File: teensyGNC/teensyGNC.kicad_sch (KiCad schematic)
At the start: 42 parts, among them J1 ESC_1_PWM, J10 ToF_OF_SH, J11 Hall_1_PH, J12 Hall_2_PH, J13 Hall_3_PH, J14 Hall_4_PH, J2 5V_In_XH, J3 ESC_2_PWM, J4 Servo_1_PWM, J5 Servo_2_PWM, J6 7V4_In, J7 Ebyte, J8 LC29H, J9 Batt_Mon_GH, U1 E28-2G4T20SX, U2 4754, U3 AP2112K-3.3, U4 4494, U5 Teensy4.1

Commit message: Test fabrication
- Downloaded fabrication toolkit
- Updated LCSC Part --> LCSC Part #
- Test BOM and gerber creation using toolkit
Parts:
- C1, C3: LCSC Part C7234 -> (none); LCSC Part # (none) -> C7234
- C2, C4, C9: LCSC Part C14663 -> (none); LCSC Part # (none) -> C14663
- C5, C6: footprint Capacitor_SMD:C_0402_1005Metric -> Capacitor_SMD:C_0603_1608Metric
- C7: LCSC Part C559769 -> (none); LCSC Part # (none) -> C559769
- C8: LCSC Part C109457 -> (none); LCSC Part # (none) -> C109457
- D1: LCSC Part C135018 -> (none); LCSC Part # (none) -> C135018
- J10: LCSC Part C160390 -> (none); LCSC Part # (none) -> C160390
- J11, J12, J13, J14: LCSC Part C131339 -> (none); LCSC Part # (none) -> C131339
- J2: LCSC Part C158012 -> (none); LCSC Part # (none) -> C158012
- J6: LCSC Part C428721 -> (none); LCSC Part # (none) -> C428721
- J7: LCSC Part C6962402 -> (none); LCSC Part # (none) -> C6962402
- J9: LCSC Part C161692 -> (none); LCSC Part # (none) -> C161692
- R1, R2: LCSC Part C122970 -> (none); LCSC Part # (none) -> C122970
- R10, R11, R5, R6, R7, R8, R9: LCSC Part C5362358 -> (none); LCSC Part # (none) -> C5362358
- R12, R13: LCSC Part C4190 -> (none); LCSC Part # (none) -> C4190
- R3: LCSC Part # (none) -> C5362358
- R4: footprint Resistor_SMD:R_0402_1005Metric -> Resistor_SMD:R_0603_1608Metric; LCSC Part C17168 -> (none); LCSC Part # (none) -> C17168
- U1: LCSC Part C42464206 -> (none); LCSC Part # (none) -> C42464206
- U3: LCSC Part C51118 -> (none); LCSC Part # (none) -> C51118

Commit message: V1.0 Order placed at JLCPCB
- Some components changed to basic versions to lower cost a bit (TOTAL 96 USD!!!?? Do try and lower further for future versions, main cost seems to be extended part fees, maybe look into more hand soldered bits?)
- Some JST connectors bought on taobao and assembled myself
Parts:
- C7: LCSC Part # C559769 -> C29936
- J7: footprint Connector_Coaxial:SMA_Amphenol_132203-12_Horizontal -> Connector_Coaxial:SMA_BAT_Wireless_BWSMA-KWE-Z001; LCSC Part # C6962402 -> C496551
- R10, R11, R3, R5, R6, R7, R8, R9: LCSC Part # C5362358 -> C25804
- R4: LCSC Part # C17168 -> C95177
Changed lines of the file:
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@@
 			)
 		)
-		(property "LCSC Part #" "C17168"
+		(property "LCSC Part #" "C95177"
 			(at 86.36 73.66 90)
 			(hide yes)
@@
 			)
 		)
-		(property "LCSC Part #" "C5362358"
+		(property "LCSC Part #" "C25804"
 			(at 97.79 39.37 90)
 			(hide yes)
@@
 			)
 		)
-		(property "LCSC Part #" "C5362358"
+		(property "LCSC Part #" "C25804"
 			(at 71.12 156.21 90)
 			(hide yes)
@@
 			)
 		)
-		(property "LCSC Part #" "C559769"
+		(property "LCSC Part #" "C29936"
 			(at 115.57 93.98 90)
 			(hide yes)
@@
 			)
 		)
-		(property "LCSC Part #" "C5362358"
+		(property "LCSC Part #" "C25804"
 			(at 121.92 39.37 90)
 			(hide yes)
@@
 			)
 		)
-		(property "LCSC Part #" "C5362358"
+		(property "LCSC Part #" "C25804"
 			(at 88.9 39.37 90)
 			(hide yes)
@@
 			)
 		)
-		(property "LCSC Part #" "C5362358"
+		(property "LCSC Part #" "C25804"
 			(at 132.08 39.37 90)
 			(hide yes)
@@
 			)
 		)
-		(property "LCSC Part #" "C5362358"
+		(property "LCSC Part #" "C25804"
 			(at 124.46 119.38 90)
 			(hide yes)
@@
 			)
 		)
-		(property "Footprint" "Connector_Coaxial:SMA_Amphenol_132203-12_Horizontal"
+		(property "Footprint" "Connector_Coaxial:SMA_BAT_Wireless_BWSMA-KWE-Z001"
 			(at 101.6 73.66 0)
 			(hide yes)
@@
 			)
 		)
-		(property "LCSC Part #" "C6962402"
+		(property "LCSC Part #" "C496551"
 			(at 101.6 73.66 0)
 			(hide yes)
@@
 			)
 		)
-		(property "LCSC Part #" "C5362358"
+		(property "LCSC Part #" "C25804"
 			(at 107.95 39.37 90)
 			(hide yes)
@@
 			)
 		)
-		(property "LCSC Part #" "C5362358"
+		(property "LCSC Part #" "C25804"
 			(at 114.3 119.38 90)
 			(hide yes)

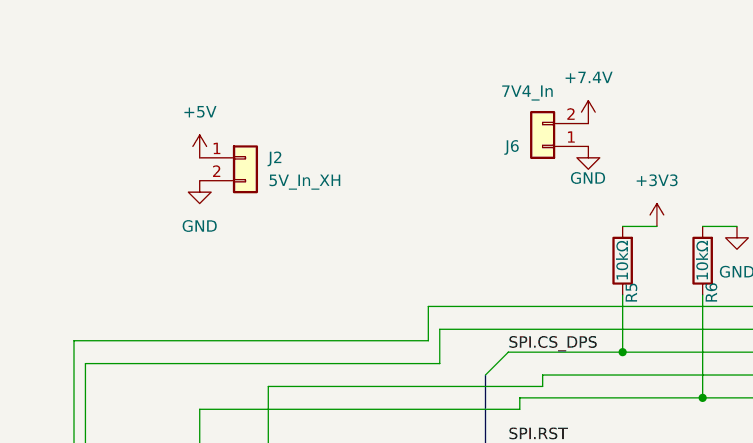
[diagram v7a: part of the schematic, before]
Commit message: ! CRITICAL FIX !
5V Input plug was placed the wrong way around, now flipped back to the correct direction on the board. For the V1.0 deliveries, the first board might have had its ebyte power voltage converter fried (not tested yet), jst xh flipped manually (steps in notebook) for successful testing of altitude control on vehicle. For second board, will need to flip the jst xh first.
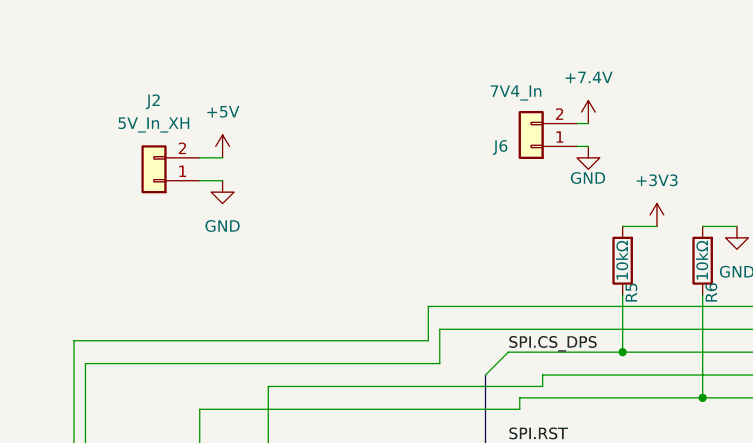
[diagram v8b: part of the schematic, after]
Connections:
- net +5V: now also J2.2 (Pin_2); no longer J2.1 (Pin_1)
- net GND: now also J2.1 (Pin_1); no longer J2.2 (Pin_2)
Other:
- moved on the sheet: J2, J6
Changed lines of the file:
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@@
 	(wire
 		(pts
+			(xy 83.82 24.13) (xy 85.09 24.13)
+		)
+		(stroke
+			(width 0)
+			(type default)
+		)
+	)
+	(wire
+		(pts
 			(xy 78.74 100.33) (xy 78.74 105.41)
 		)
@@
 	(wire
 		(pts
+			(xy 44.45 30.48) (xy 41.91 30.48)
+		)
+		(stroke
+			(width 0)
+			(type default)
+		)
+	)
+	(wire
+		(pts
 			(xy 25.4 172.72) (xy 82.55 172.72)
 		)
@@
 	(wire
 		(pts
+			(xy 44.45 27.94) (xy 41.91 27.94)
+		)
+		(stroke
+			(width 0)
+			(type default)
+		)
+	)
+	(wire
+		(pts
 			(xy 132.08 35.56) (xy 135.89 35.56)
 		)
@@
 	(wire
 		(pts
+			(xy 83.82 26.67) (xy 85.09 26.67)
+		)
+		(stroke
+			(width 0)
+			(type default)
+		)
+	)
+	(wire
+		(pts
 			(xy 213.36 57.15) (xy 213.36 73.66)
 		)
@@
 	(symbol
 		(lib_id "Connector_Generic:Conn_01x02")
-		(at 46.99 27.94 0)
+		(at 36.83 30.48 180)
 		(unit 1)
 		(body_style 1)
@@
 		(fields_autoplaced yes)
 		(property "Reference" "J2"
-			(at 49.53 27.9399 0)
+			(at 36.83 21.59 0)
 			(show_name no)
 			(do_not_autoplace no)
@@
 					(size 1.27 1.27)
 				)
-				(justify left)
 			)
 		)
 		(property "Value" "5V_In_XH"
-			(at 49.53 30.4799 0)
+			(at 36.83 24.13 0)
 			(show_name no)
 			(do_not_autoplace no)
@@
 					(size 1.27 1.27)
 				)
-				(justify left)
 			)
 		)
 		(property "Footprint" "Connector_JST:JST_XH_B2B-XH-AM_1x02_P2.50mm_Vertical"
-			(at 46.99 27.94 0)
+			(at 36.83 30.48 0)
 			(hide yes)
 			(show_name no)
@@
 		)
 		(property "Datasheet" ""
-			(at 46.99 27.94 0)
+			(at 36.83 30.48 0)
 			(hide yes)
 			(show_name no)
@@
 		)
 		(property "Description" "Generic connector, single row, 01x02, script generated (kicad-library-utils/schlib/autogen/connector/)"
-			(at 46.99 27.94 0)
+			(at 36.83 30.48 0)
 			(hide yes)
 			(show_name no)
@@
 		)
 		(property "LCSC Part #" "C158012"
-			(at 46.99 27.94 0)
+			(at 36.83 30.48 0)
 			(hide yes)
 			(show_name no)
@@
 		)
 		(property "LCSC Part" ""
-			(at 46.99 27.94 0)
+			(at 36.83 30.48 0)
 			(hide yes)
 			(show_name no)
@@
 	(symbol
 		(lib_id "power:GND")
-		(at 41.91 30.48 0)
+		(at 44.45 30.48 0)
 		(unit 1)
 		(body_style 1)
@@
 		(fields_autoplaced yes)
 		(property "Reference" "#PWR05"
-			(at 41.91 36.83 0)
+			(at 44.45 36.83 0)
 			(hide yes)
 			(show_name no)
@@
 		)
 		(property "Value" "GND"
-			(at 41.91 35.56 0)
+			(at 44.45 35.56 0)
 			(show_name no)
 			(do_not_autoplace no)
@@
 		)
 		(property "Footprint" ""
-			(at 41.91 30.48 0)
+			(at 44.45 30.48 0)
 			(hide yes)
 			(show_name no)
@@
 		)
 		(property "Datasheet" ""
-			(at 41.91 30.48 0)
+			(at 44.45 30.48 0)
 			(hide yes)
 			(show_name no)
@@
 		)
 		(property "Description" "Power symbol creates a global label with name \"GND\" , ground"
-			(at 41.91 30.48 0)
+			(at 44.45 30.48 0)
 			(hide yes)
 			(show_name no)
@@
 	(symbol
 		(lib_id "power:+5V")
-		(at 41.91 27.94 0)
+		(at 44.45 27.94 0)
 		(unit 1)
 		(body_style 1)
@@
 		(fields_autoplaced yes)
 		(property "Reference" "#PWR04"
-			(at 41.91 31.75 0)
+			(at 44.45 31.75 0)
 			(hide yes)
 			(show_name no)
@@
 		)
 		(property "Value" "+5V"
-			(at 41.91 22.86 0)
+			(at 44.45 22.86 0)
 			(show_name no)
 			(do_not_autoplace no)
@@
 		)
 		(property "Footprint" ""
-			(at 41.91 27.94 0)
+			(at 44.45 27.94 0)
 			(hide yes)
 			(show_name no)
@@
 		)
 		(property "Datasheet" ""
-			(at 41.91 27.94 0)
+			(at 44.45 27.94 0)
 			(hide yes)
 			(show_name no)
@@
 		)
 		(property "Description" "Power symbol creates a global label with name \"+5V\""
-			(at 41.91 27.94 0)
+			(at 44.45 27.94 0)
 			(hide yes)
 			(show_name no)
@@
 	(symbol
 		(lib_id "Connector_Generic:Conn_01x02")
-		(at 80.01 26.67 180)
+		(at 78.74 26.67 180)
 		(unit 1)
 		(body_style 1)
@@
 		(dnp no)
 		(property "Reference" "J6"
-			(at 77.47 26.6701 0)
+			(at 76.2 26.6701 0)
 			(show_name no)
 			(do_not_autoplace no)
@@
 		)
 		(property "Value" "7V4_In"
-			(at 81.28 20.574 0)
+			(at 80.01 20.574 0)
 			(show_name no)
 			(do_not_autoplace no)
@@
 		)
 		(property "Footprint" "Connector_AMASS:AMASS_XT30UPB-M_1x02_P5.0mm_Vertical"
-			(at 80.01 26.67 0)
+			(at 78.74 26.67 0)
 			(hide yes)
 			(show_name no)
@@
 		)
 		(property "Datasheet" ""
-			(at 80.01 26.67 0)
+			(at 78.74 26.67 0)
 			(hide yes)
 			(show_name no)
@@
 		)
 		(property "Description" "Generic connector, single row, 01x02, script generated (kicad-library-utils/schlib/autogen/connector/)"
-			(at 80.01 26.67 0)
+			(at 78.74 26.67 0)
 			(hide yes)
 			(show_name no)
@@
 		)
 		(property "LCSC Part #" "C428721"
-			(at 80.01 26.67 0)
+			(at 78.74 26.67 0)
 			(hide yes)
 			(show_name no)
@@
 		)
 		(property "LCSC Part" ""
-			(at 80.01 26.67 0)
+			(at 78.74 26.67 0)
 			(hide yes)
 			(show_name no)
